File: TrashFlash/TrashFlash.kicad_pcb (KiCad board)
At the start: 6 copper layers, 108 x 60 mm, 152 parts, among them IC201 AD8615AUJZ-REEL, IC202 ADG5419BCPZ-RL7, IC203 SN74LXC2T45QDTTRQ1, IC301 LTC3643IUDD#PBF, IC401 STM32L471QEI6, IC501 TPS63900DSKR, IC502 TPS63900DSKR, IC601 LP5024RSMR, IC602 PEC11S-929K-S0015, IC701 BQ27426YZFR, IC702 BQ24230RGTR, IC703 BQ29732DSER, IC801 CC110LRGPR, J101 15130322601000, J102 15230322601000, J103 FTSH-107-01-L-DV-K-A, J701 USB4800-03-A, Q201 BC56-10PA,115, Q202 BC56-10PA,115, Q203 BC56-10PA,115, Q204 BC56-10PA,115, Q701 PMDPB30XNAX, U201 SI5448DU-T1-GE3, U202 SI5448DU-T1-GE3, Y401 ECS-160-8-33B2-CTN-TR3, Y801 ECS-260-10-33B-CKM-TR

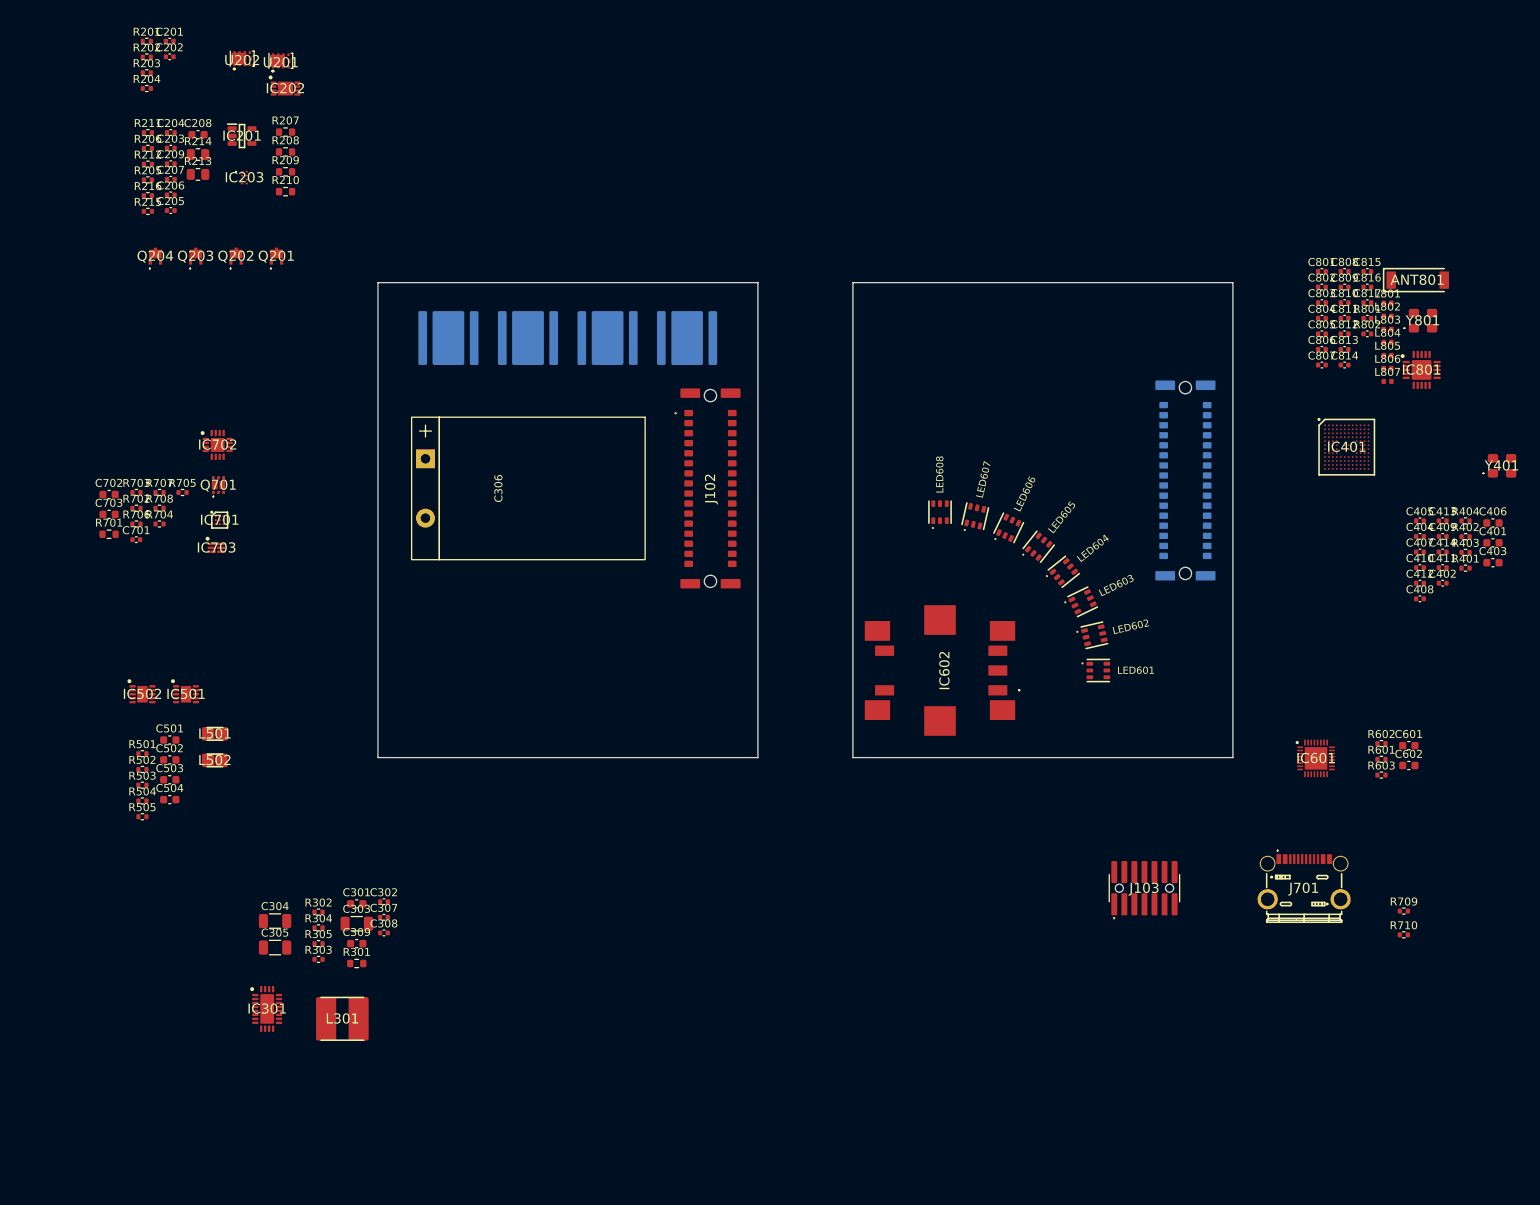
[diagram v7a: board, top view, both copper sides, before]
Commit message: Added Caps to Battery Charger
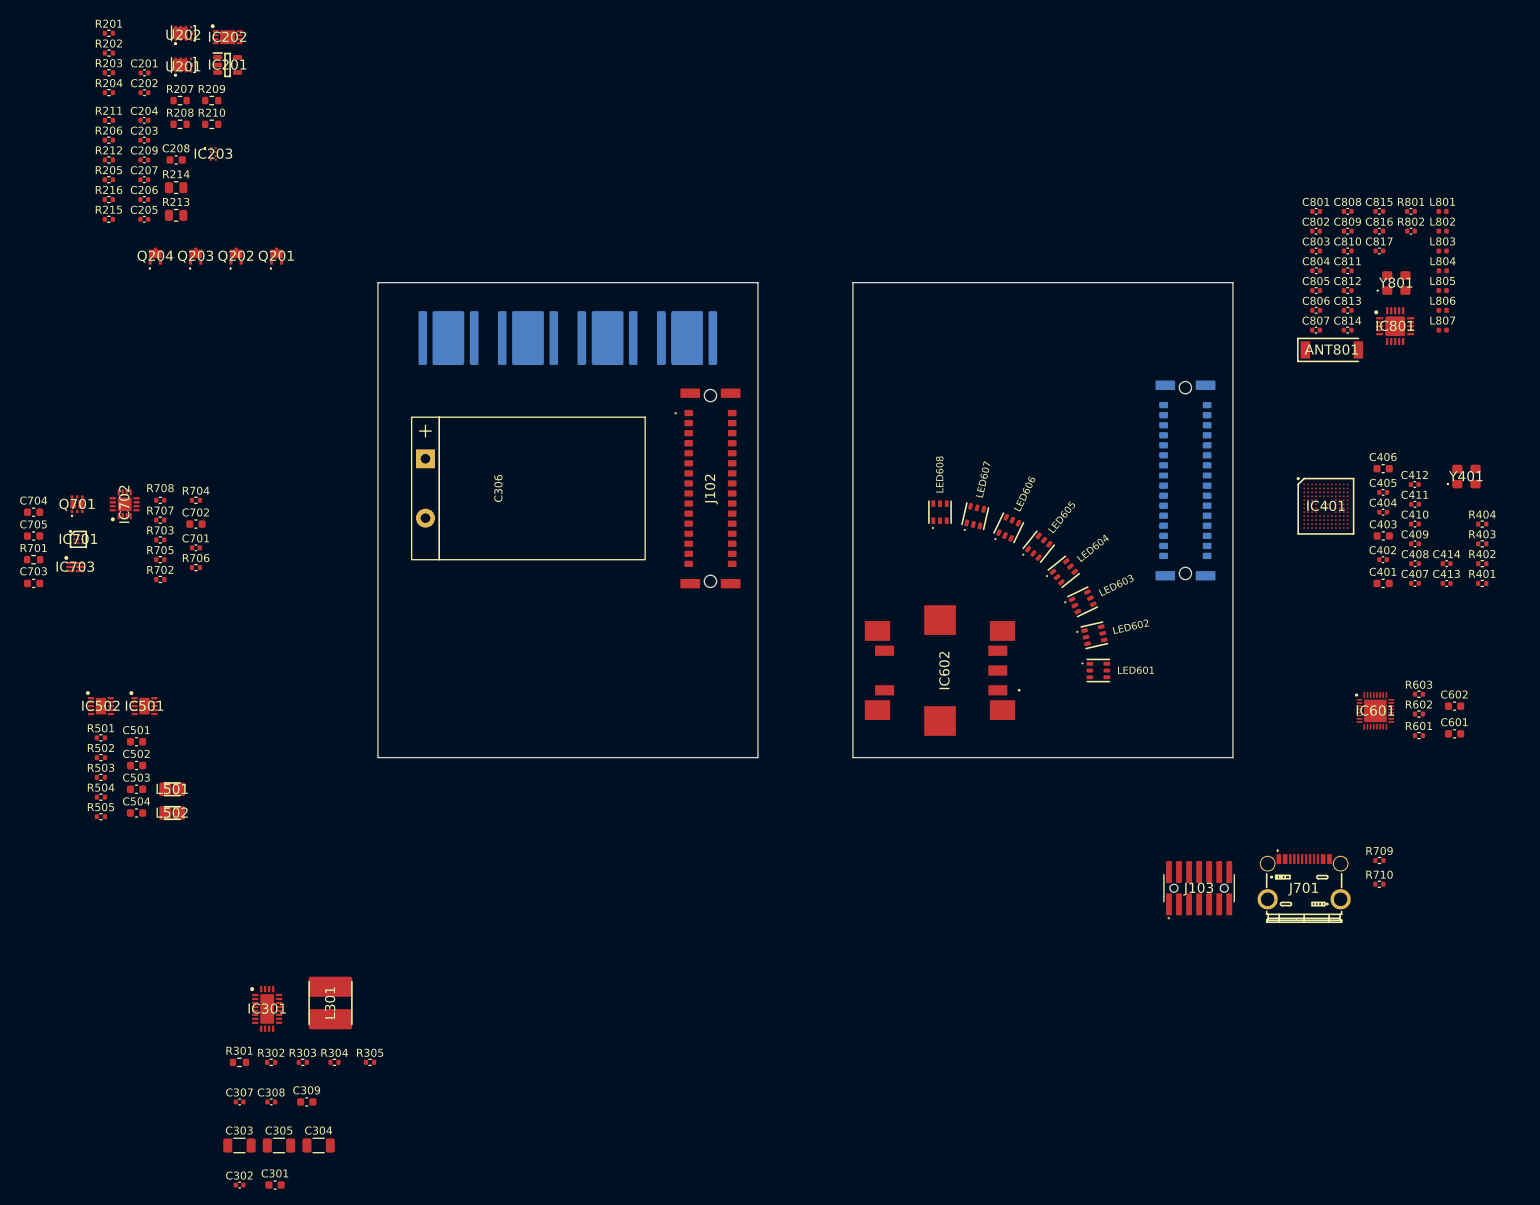
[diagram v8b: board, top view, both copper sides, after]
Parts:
- added C704: 4.7u, Capacitor_SMD:C_0603_1608Metric, F.Cu at (56.5, 129.0)
- added C705: 1u, Capacitor_SMD:C_0603_1608Metric, F.Cu at (56.5, 132.0)
- C703: value 1u -> 4.7u
- moved C302 40.2 mm to (82.5, 214.0)
- moved C301 37.0 mm to (87.0, 214.0)
- moved C303 31.7 mm to (82.5, 209.0)
- moved C307 29.6 mm to (82.5, 203.5)
- moved C304 28.9 mm to (92.5, 209.0)
- moved C308 25.7 mm to (86.5, 203.5)
- moved C305 25.0 mm to (87.5, 209.0)
- moved C309 21.0 mm to (91.0, 203.5)
- moved R302 19.9 mm to (86.5, 198.5)
- moved R301 19.4 mm to (82.5, 198.5)
- moved IC701 18.0 mm to (62.1, 132.4)
- moved IC703 18.0 mm to (61.8, 135.9)
- moved Q701 18.0 mm to (62.0, 128.0)
- moved R304 17.1 mm to (94.5, 198.5)
- moved R305 16.4 mm to (99.0, 198.5)
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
